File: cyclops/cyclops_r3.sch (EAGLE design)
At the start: 140 parts, among them Q1 BC817, Q2 IRF510, Q3 BC817, T0 0, T1 0, T2 0, T3 0, U1 MCP4921, U10 TLV2374, U11 THS4281, U12 MAX4564, U13 ZXTD, U14 ZXTD, U2 ADG3301, U3 MAX4564, U4 LT1931, U5 LT1764A, U6 337L, U7 TLV3701, U8 ADR03, U9 OP1177, X1 SLP3, X2 SLP3, X3 SLP3

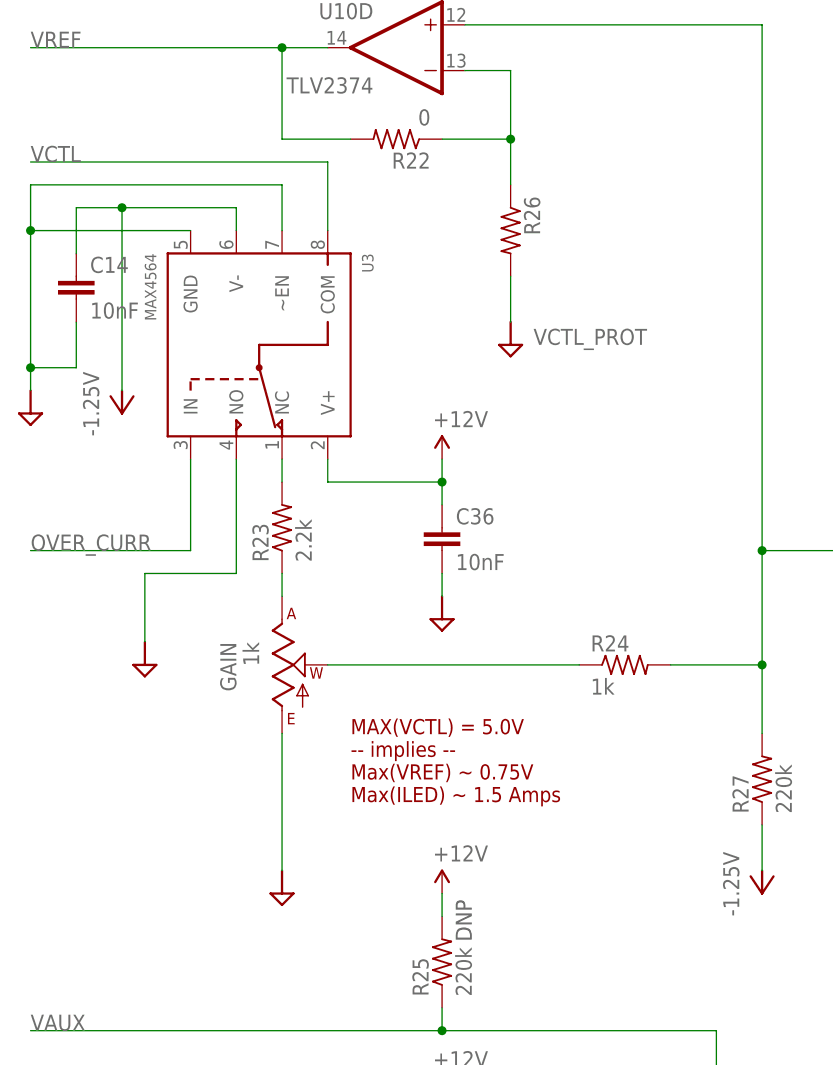
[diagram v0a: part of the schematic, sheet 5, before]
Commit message: Addeda jumper to bypass the oc switch circuit.
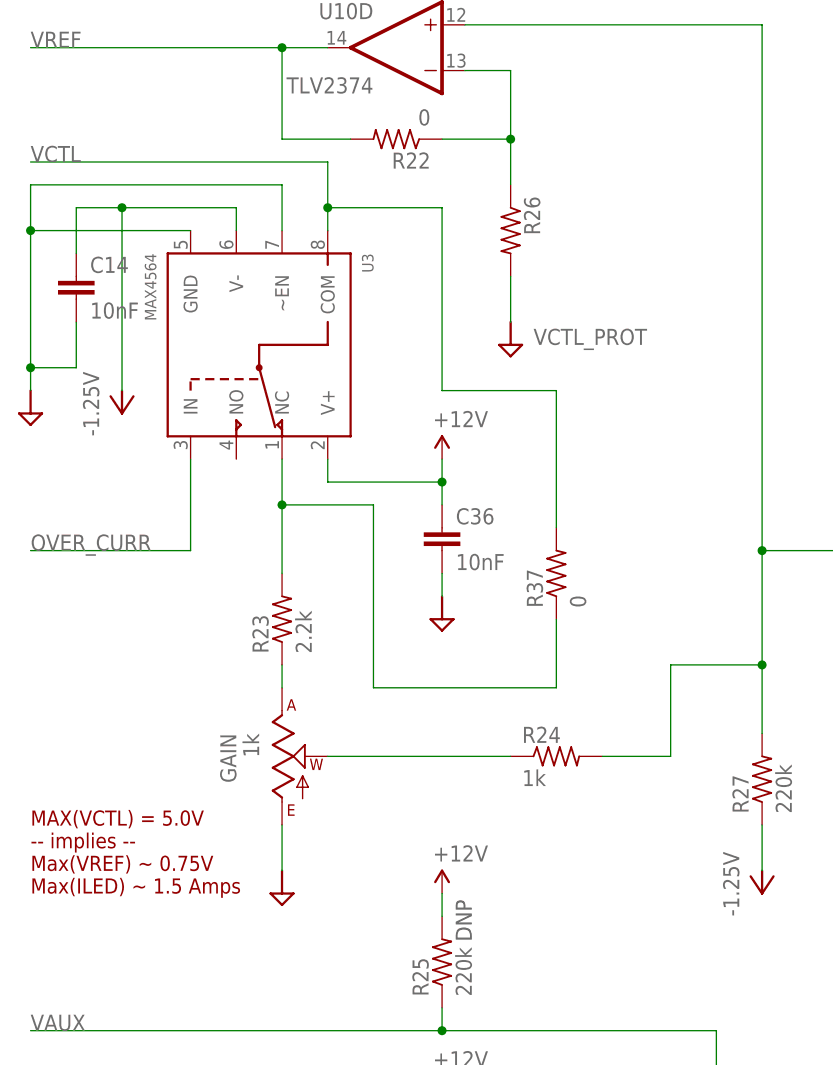
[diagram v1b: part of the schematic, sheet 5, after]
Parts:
- added R37: 0, cyclops:R_0603
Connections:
- net GND: no longer U3.NO
- net VCTL: now also R37.2
- net VCTL_PROT: now also R37.1
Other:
- moved on the sheet: GAIN, R23, R24
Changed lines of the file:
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@@
 <part name="U3" library="cyclops" deviceset="MAX4564" device=""/>
 <part name="SUPPLY12" library="cyclops" deviceset="+12V" device=""/>
-<part name="U$48" library="cyclops" deviceset="GND2" device=""/>
 <part name="R21" library="cyclops" deviceset="R" device="_0603" value="10k"/>
 <part name="U$62" library="cyclops" deviceset="GND1" device=""/>
@@
 <part name="OC0" library="cyclops" deviceset="R" device="_0603" value="0"/>
 <part name="OC3" library="cyclops" deviceset="R" device="_0603" value="0"/>
+<part name="R37" library="cyclops" deviceset="R" device="_0603" value="0"/>
 </parts>
 <sheets>
@@
 <vertex x="158.496" y="50.546"/>
 </polygon>
-<text x="-45.72" y="60.96" size="1.6764" layer="94">MAX(VCTL) = 5.0V
+<text x="-81.28" y="50.8" size="1.6764" layer="94">MAX(VCTL) = 5.0V
 -- implies --
 Max(VREF) ~ 0.75V
@@
 <instance part="C28" gate="C" x="-17.78" y="-10.16"/>
 <instance part="C26" gate="C" x="-25.4" y="-10.16"/>
-<instance part="GAIN" gate="G$1" x="-53.34" y="76.2" rot="MR180"/>
+<instance part="GAIN" gate="G$1" x="-53.34" y="66.04" rot="MR180"/>
 <instance part="U$22" gate="G$1" x="-25.4" y="-20.32"/>
 <instance part="U$23" gate="G$1" x="-17.78" y="-20.32"/>
@@
 <instance part="U$29" gate="G$1" x="165.1" y="-38.1"/>
 <instance part="P-1" gate="1" x="-35.56" y="-20.32"/>
-<instance part="R23" gate="R" x="-53.34" y="91.44" rot="R90"/>
+<instance part="R23" gate="R" x="-53.34" y="81.28" rot="R90"/>
 <instance part="HEATSINK" gate="G$1" x="175.26" y="93.98" smashed="yes" rot="R270">
 <attribute name="NAME" x="175.26" y="95.25" size="1.27" layer="95"/>
@@
 <instance part="U14" gate="G$2" x="99.06" y="68.58"/>
 <instance part="SUPPLY14" gate="G$1" x="78.74" y="83.82"/>
-<instance part="R24" gate="R" x="-15.24" y="76.2"/>
+<instance part="R24" gate="R" x="-22.86" y="66.04"/>
 <instance part="P-6" gate="1" x="22.86" y="55.88"/>
 <instance part="C32" gate="C" x="30.48" y="48.26" rot="R90"/>
@@
 <instance part="U3" gate="G$1" x="-55.88" y="111.76" rot="R270"/>
 <instance part="SUPPLY12" gate="G$1" x="-35.56" y="99.06"/>
-<instance part="U$48" gate="G$1" x="-68.58" y="76.2"/>
+<instance part="R37" gate="R" x="-22.86" y="86.36" rot="R90"/>
 </instances>
 <busses>
@@
 <net name="GND" class="0">
 <segment>
-<wire x1="-53.34" y1="68.58" x2="-53.34" y2="53.34" width="0.1524" layer="91"/>
+<wire x1="-53.34" y1="58.42" x2="-53.34" y2="53.34" width="0.1524" layer="91"/>
 <pinref part="GAIN" gate="G$1" pin="E"/>
 </segment>
@@
 <wire x1="-76.2" y1="109.22" x2="-81.28" y2="109.22" width="0.1524" layer="91"/>
 <junction x="-81.28" y="109.22"/>
-</segment>
-<segment>
-<pinref part="U3" gate="G$1" pin="NO"/>
-<wire x1="-58.42" y1="99.06" x2="-58.42" y2="86.36" width="0.1524" layer="91"/>
-<wire x1="-58.42" y1="86.36" x2="-68.58" y2="86.36" width="0.1524" layer="91"/>
-<wire x1="-68.58" y1="86.36" x2="-68.58" y2="78.74" width="0.1524" layer="91"/>
 </segment>
 <segment>
@@
 <pinref part="U11" gate="G$1" pin="+IN"/>
 <pinref part="R24" gate="R" pin="2"/>
+<wire x1="-17.78" y1="66.04" x2="-10.16" y2="66.04" width="0.1524" layer="91"/>
+<wire x1="-10.16" y1="66.04" x2="-10.16" y2="76.2" width="0.1524" layer="91"/>
 <wire x1="-10.16" y1="76.2" x2="0" y2="76.2" width="0.1524" layer="91"/>
 <wire x1="0" y1="76.2" x2="0" y2="88.9" width="0.1524" layer="91"/>
@@
 <pinref part="GAIN" gate="G$1" pin="A"/>
 <pinref part="R23" gate="R" pin="1"/>
-<wire x1="-53.34" y1="83.82" x2="-53.34" y2="86.36" width="0.1524" layer="91"/>
+<wire x1="-53.34" y1="73.66" x2="-53.34" y2="76.2" width="0.1524" layer="91"/>
 </segment>
 </net>
@@
 <pinref part="GAIN" gate="G$1" pin="W"/>
 <pinref part="R24" gate="R" pin="1"/>
-<wire x1="-48.26" y1="76.2" x2="-20.32" y2="76.2" width="0.1524" layer="91"/>
+<wire x1="-48.26" y1="66.04" x2="-27.94" y2="66.04" width="0.1524" layer="91"/>
 </segment>
 </net>
@@
 <pinref part="R23" gate="R" pin="2"/>
 <pinref part="U3" gate="G$1" pin="NC"/>
-<wire x1="-53.34" y1="99.06" x2="-53.34" y2="96.52" width="0.1524" layer="91"/>
+<wire x1="-53.34" y1="99.06" x2="-53.34" y2="93.98" width="0.1524" layer="91"/>
+<wire x1="-53.34" y1="93.98" x2="-53.34" y2="86.36" width="0.1524" layer="91"/>
+<wire x1="-53.34" y1="93.98" x2="-43.18" y2="93.98" width="0.1524" layer="91"/>
+<wire x1="-43.18" y1="93.98" x2="-43.18" y2="73.66" width="0.1524" layer="91"/>
+<junction x="-53.34" y="93.98"/>
+<wire x1="-43.18" y1="73.66" x2="-22.86" y2="73.66" width="0.1524" layer="91"/>
+<wire x1="-22.86" y1="73.66" x2="-22.86" y2="81.28" width="0.1524" layer="91"/>
+<pinref part="R37" gate="R" pin="1"/>
 </segment>
 </net>
@@
 <pinref part="U3" gate="G$1" pin="COM"/>
 <wire x1="-81.28" y1="132.08" x2="-48.26" y2="132.08" width="0.1524" layer="91"/>
-<wire x1="-48.26" y1="132.08" x2="-48.26" y2="124.46" width="0.1524" layer="91"/>
+<wire x1="-48.26" y1="132.08" x2="-48.26" y2="127" width="0.1524" layer="91"/>
 <label x="-81.28" y="132.08" size="1.778" layer="95"/>
-</segment>
-</net>
+<wire x1="-48.26" y1="127" x2="-48.26" y2="124.46" width="0.1524" layer="91"/>
+<wire x1="-48.26" y1="127" x2="-35.56" y2="127" width="0.1524" layer="91"/>
+<wire x1="-35.56" y1="127" x2="-35.56" y2="106.68" width="0.1524" layer="91"/>
+<junction x="-48.26" y="127"/>
+<pinref part="R37" gate="R" pin="2"/>
+<wire x1="-35.56" y1="106.68" x2="-22.86" y2="106.68" width="0.1524" layer="91"/>
+<wire x1="-22.86" y1="106.68" x2="-22.86" y2="91.44" width="0.1524" layer="91"/>
+</segment>
+</net>

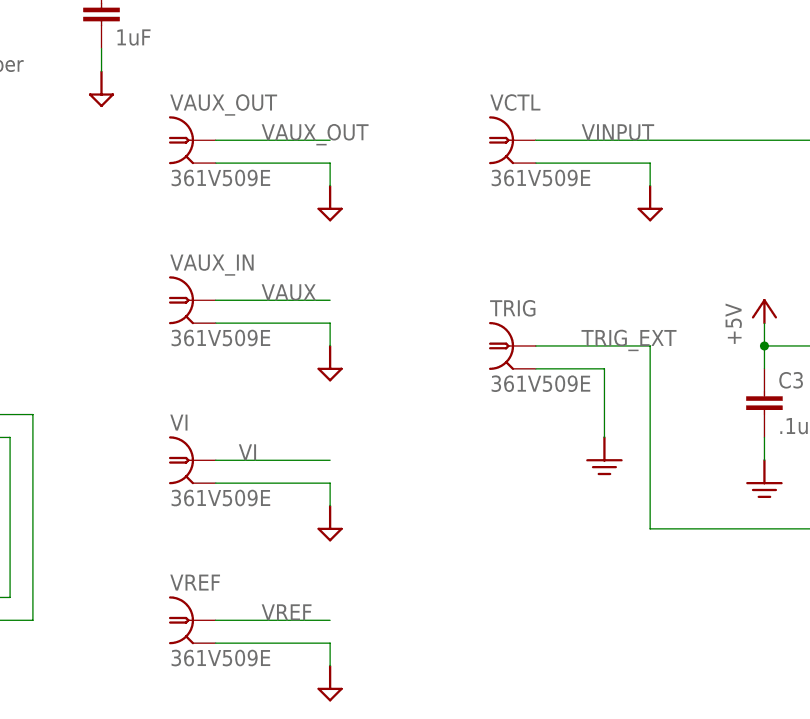
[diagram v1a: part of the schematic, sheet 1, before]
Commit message: Replaced edge mount BNC with cheaper alternative
- Less than half the price
- Much more available (made by molex)
- Huge BOM money saver
- Worried about production run with this many changes...
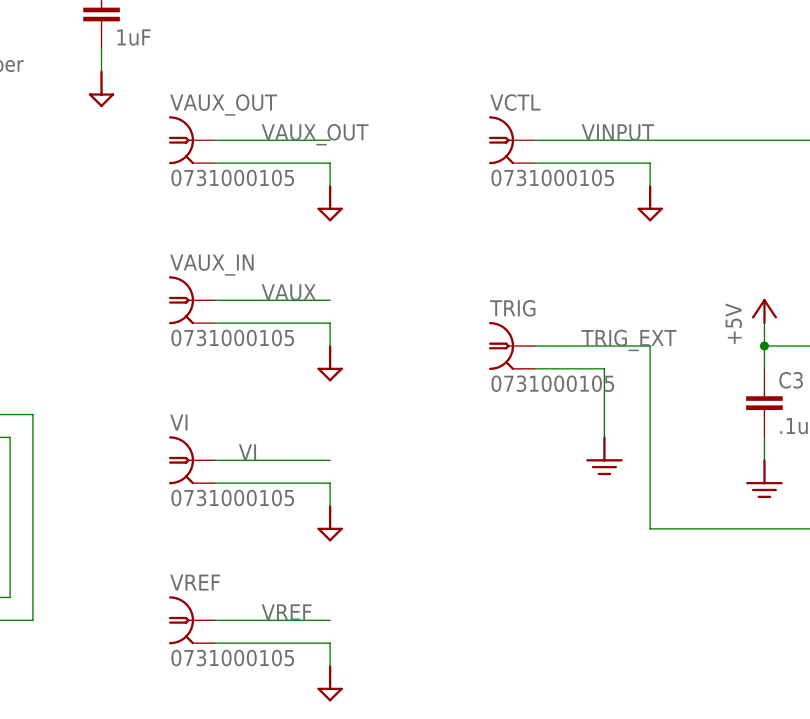
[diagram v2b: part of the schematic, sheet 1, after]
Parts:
- TRIG, VAUX_IN, VAUX_OUT, VCTL, VI, VREF: value 361V509E -> 0731000105; device cyclops:BNC_V-BITE -> jonnew:BNC_0731000105
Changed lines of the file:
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@@
 <part name="TEST" library="cyclops" deviceset="SPDT" device="_CFPA" value="CFPA"/>
 <part name="Q2" library="cyclops" deviceset="N-MOSFET" device="TO-262" value="IRF510"/>
-<part name="VAUX_OUT" library="cyclops" deviceset="BNC" device="_V-BITE" value="361V509E"/>
+<part name="VAUX_OUT" library="jonnew" deviceset="BNC" device="_0731000105" value="0731000105"/>
 <part name="REF2.5" library="cyclops" deviceset="TP" device="TP16R" value="TPTP16R"/>
 <part name="REF5.0" library="cyclops" deviceset="TP" device="TP16R" value="TPTP16R"/>
@@
 <part name="Q1" library="cyclops" deviceset="BC817*" device="SMD" technology="-16" value="BC817"/>
 <part name="R14" library="cyclops" deviceset="R" device="_0603" value="10k"/>
-<part name="VI" library="cyclops" deviceset="BNC" device="_V-BITE" value="361V509E"/>
-<part name="VREF" library="cyclops" deviceset="BNC" device="_V-BITE" value="361V509E"/>
-<part name="VCTL" library="cyclops" deviceset="BNC" device="_V-BITE" value="361V509E"/>
+<part name="VI" library="jonnew" deviceset="BNC" device="_0731000105" value="0731000105"/>
+<part name="VREF" library="jonnew" deviceset="BNC" device="_0731000105" value="0731000105"/>
+<part name="VCTL" library="jonnew" deviceset="BNC" device="_0731000105" value="0731000105"/>
 <part name="PWR_DIST" library="cyclops" deviceset="PINH2X4" device=""/>
 <part name="GAIN" library="cyclops" deviceset="POT_US" device="_3310" value="1k"/>
@@
 <part name="L2" library="cyclops" deviceset="L" device="_0603" value="MPZ1608"/>
 <part name="EXPANSION" library="cyclops" deviceset="PINH2X5" device="_ICD-H"/>
-<part name="VAUX_IN" library="cyclops" deviceset="BNC" device="_V-BITE" value="361V509E"/>
+<part name="VAUX_IN" library="jonnew" deviceset="BNC" device="_0731000105" value="0731000105"/>
 <part name="U$1" library="cyclops" deviceset="GND2" device=""/>
 <part name="U$2" library="cyclops" deviceset="GND2" device=""/>
@@
 <part name="P-2" library="cyclops" deviceset="-5V" device="" value="-1.25V"/>
 <part name="R25" library="cyclops" deviceset="R" device="_0603" value="220k"/>
-<part name="TRIG" library="cyclops" deviceset="BNC" device="_V-BITE" value="361V509E"/>
+<part name="TRIG" library="jonnew" deviceset="BNC" device="_0731000105" value="0731000105"/>
 <part name="U$47" library="cyclops" deviceset="GND1" device=""/>
 <part name="LEO-HEADERS" library="cyclops" deviceset="ARDUINO_HEADER_SET" device=""/>
